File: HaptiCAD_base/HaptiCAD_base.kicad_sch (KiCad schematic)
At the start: 1 part

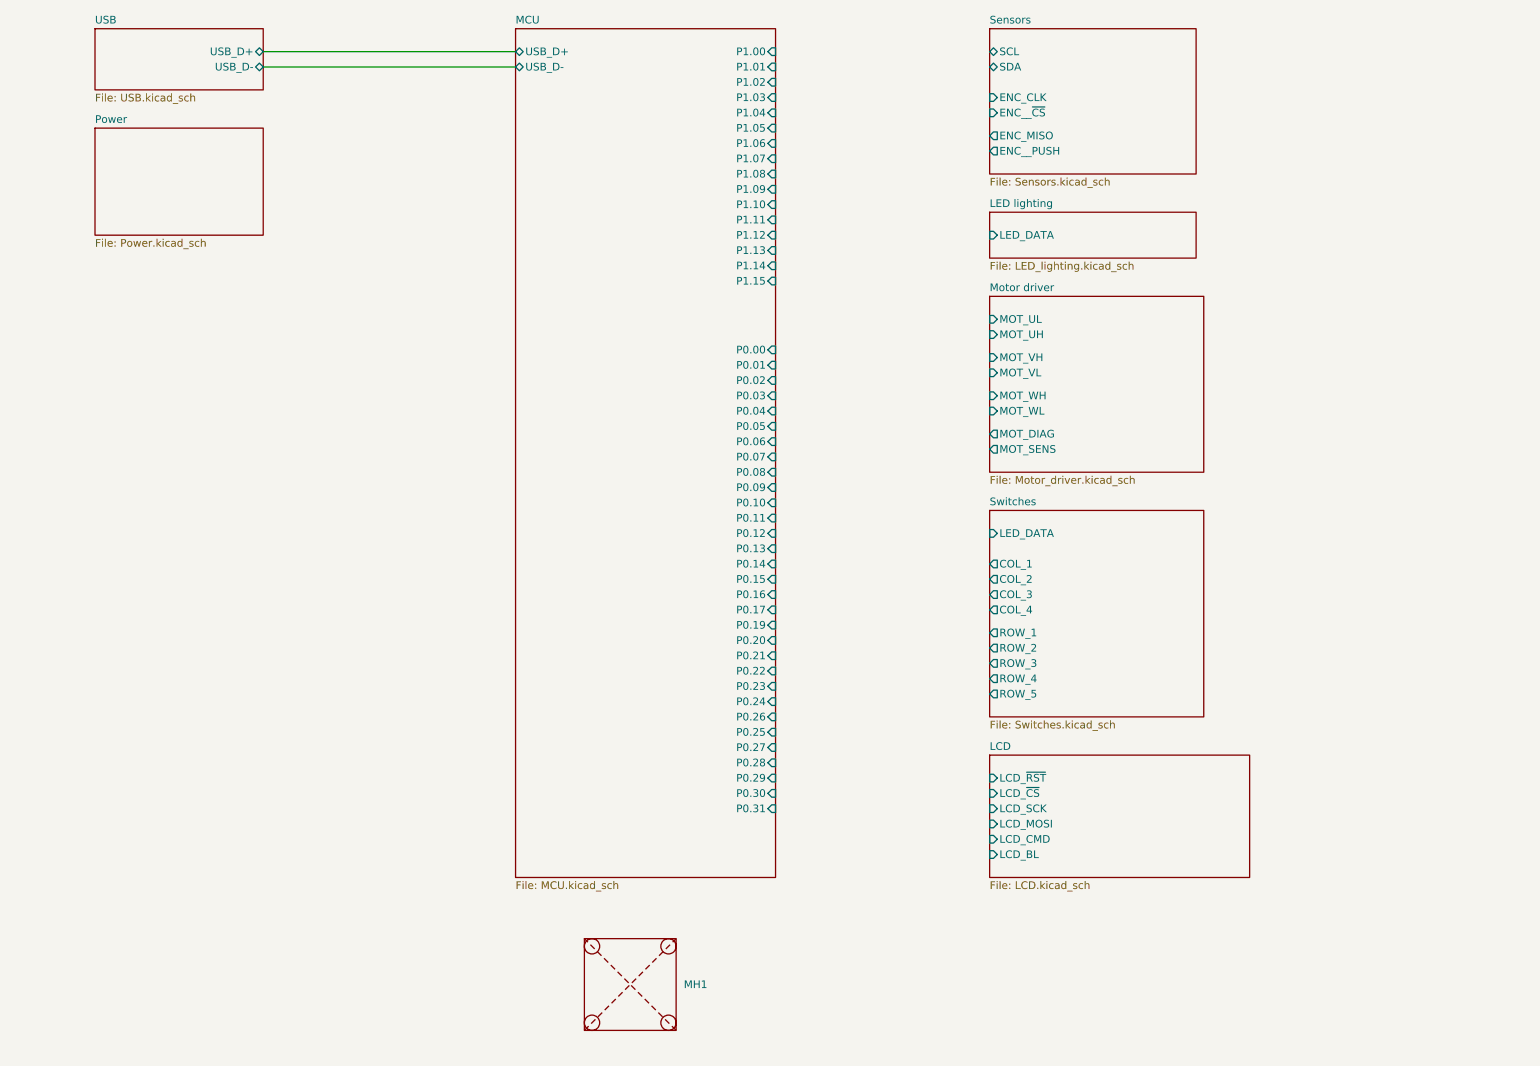
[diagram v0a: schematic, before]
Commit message: Split project into base and motor mount pcb
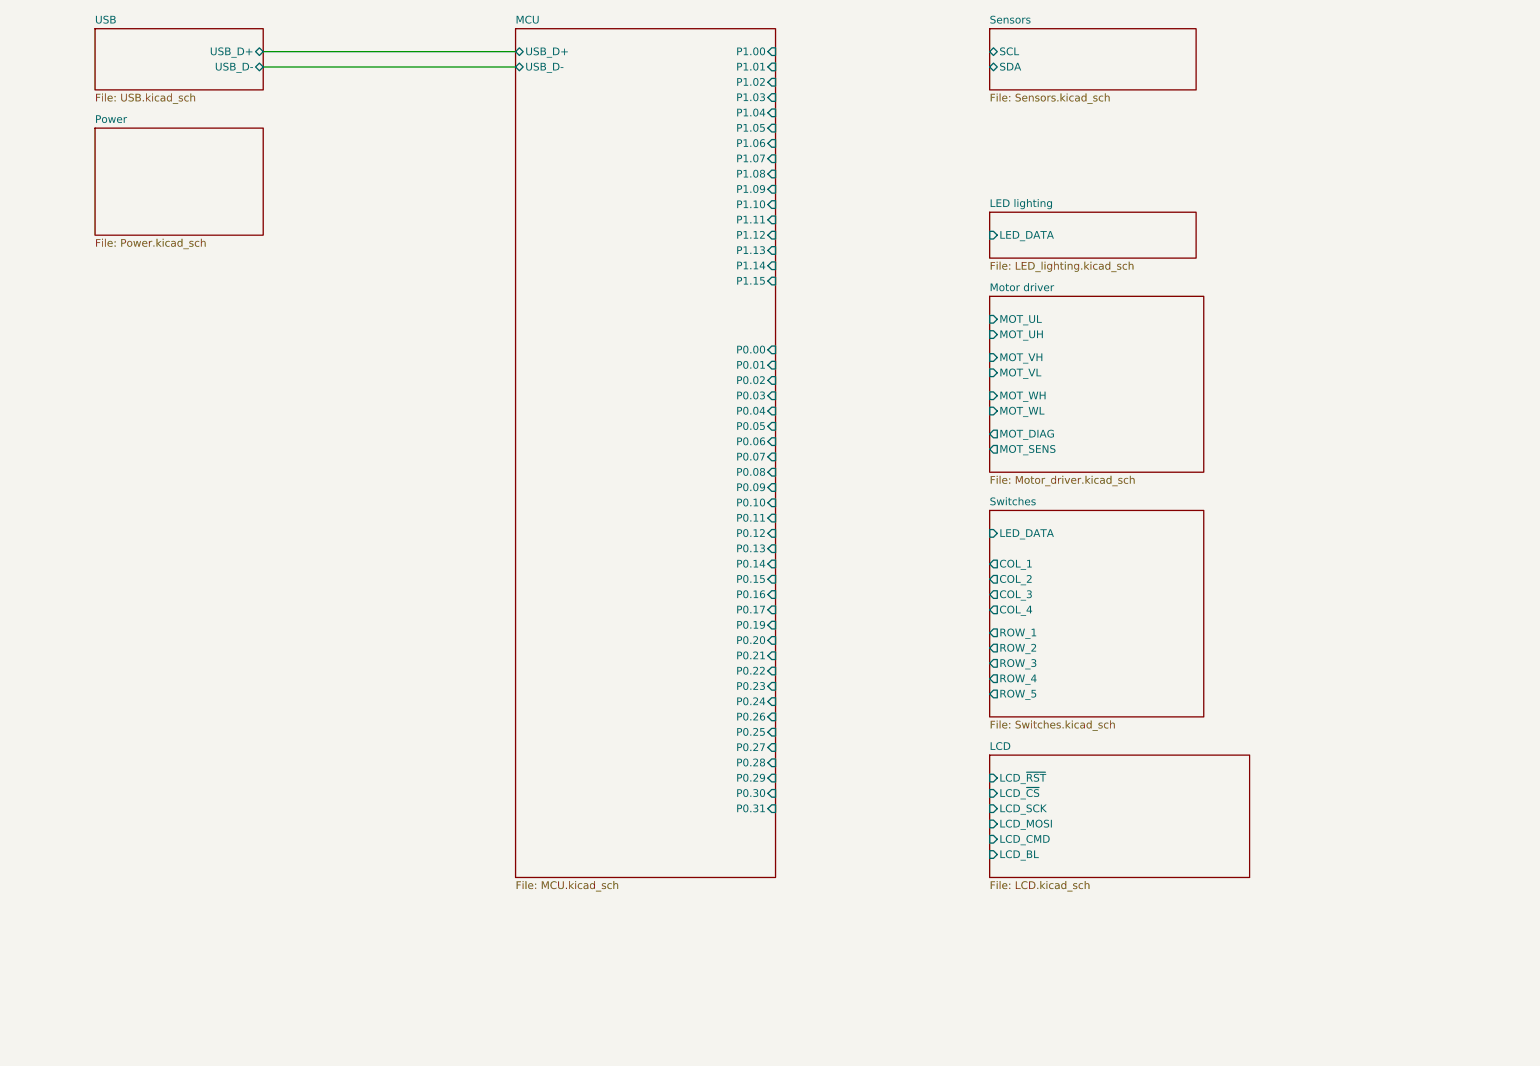
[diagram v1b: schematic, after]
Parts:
- removed MH1: (no value), BLDC_mount:BLDC_mount, symbol BLDC_mount:BLDC_mount
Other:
- sheet Sensors ports: added none; removed ENC_CLK, ENC_MISO, ENC__PUSH, ENC__~{CS}
- title: Knobber -> Base
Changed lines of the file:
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@@
 	(paper "A4")
 	(title_block
-		(title "Knobber")
+		(title "Base")
 		(date "2026-03-16")
 		(rev "V0.1")
@@
 		)
 	)
-	(symbol
-		(lib_id "BLDC_mount:BLDC_mount")
-		(at 135.89 180.34 0)
-		(unit 1)
-		(body_style 1)
-		(exclude_from_sim yes)
+	(sheet
+		(at 195.58 142.24)
+		(size 43.18 20.32)
+		(exclude_from_sim no)
 		(in_bom no)
-		(on_board yes)
-		(in_pos_files yes)
-		(dnp no)
+		(on_board no)
+		(dnp yes)
 		(fields_autoplaced yes)
-		(property "Reference" "MH1"
-			(at 144.78 180.3399 0)
-			(show_name no)
-			(do_not_autoplace no)
-			(effects
-				(font
-					(size 1.27 1.27)
-				)
-				(justify left)
-			)
-		)
-		(property "Value" ""
-			(at 135.89 180.34 0)
-			(show_name no)
-			(do_not_autoplace no)
-			(effects
-				(font
-					(size 1.27 1.27)
-				)
-			)
-		)
-		(property "Footprint" "BLDC_mount:BLDC_mount"
-			(at 135.89 180.34 0)
-			(hide yes)
-			(show_name no)
-			(do_not_autoplace no)
-			(effects
-				(font
-					(size 1.27 1.27)
-				)
-			)
-		)
-		(property "Datasheet" ""
-			(at 135.89 180.34 0)
-			(hide yes)
-			(show_name no)
-			(do_not_autoplace no)
-			(effects
-				(font
-					(size 1.27 1.27)
-				)
-			)
-		)
-		(property "Description" ""
-			(at 135.89 180.34 0)
-			(hide yes)
-			(show_name no)
-			(do_not_autoplace no)
-			(effects
-				(font
-					(size 1.27 1.27)
-				)
+		(stroke
+			(width 0.1524)
+			(type solid)
+		)
+		(fill
+			(color 0 0 0 0)
+		)
+		(property "Sheetname" "LCD"
+			(at 195.58 141.5284 0)
+			(show_name no)
+			(do_not_autoplace no)
+			(effects
+				(font
+					(size 1.27 1.27)
+				)
+				(justify left bottom)
+			)
+		)
+		(property "Sheetfile" "LCD.kicad_sch"
+			(at 195.58 163.1446 0)
+			(show_name no)
+			(do_not_autoplace no)
+			(effects
+				(font
+					(size 1.27 1.27)
+				)
+				(justify left top)
+			)
+		)
+		(pin "LCD_BL" input
+			(at 195.58 158.75 180)
+			(effects
+				(font
+					(size 1.27 1.27)
+				)
+				(justify left)
+			)
+		)
+		(pin "LCD_CMD" input
+			(at 195.58 156.21 180)
+			(effects
+				(font
+					(size 1.27 1.27)
+				)
+				(justify left)
+			)
+		)
+		(pin "LCD_MOSI" input
+			(at 195.58 153.67 180)
+			(effects
+				(font
+					(size 1.27 1.27)
+				)
+				(justify left)
+			)
+		)
+		(pin "LCD_SCK" input
+			(at 195.58 151.13 180)
+			(effects
+				(font
+					(size 1.27 1.27)
+				)
+				(justify left)
+			)
+		)
+		(pin "LCD_~{CS}" input
+			(at 195.58 148.59 180)
+			(effects
+				(font
+					(size 1.27 1.27)
+				)
+				(justify left)
+			)
+		)
+		(pin "LCD_~{RST}" input
+			(at 195.58 146.05 180)
+			(effects
+				(font
+					(size 1.27 1.27)
+				)
+				(justify left)
 			)
 		)
 		(instances
-			(project "knobber"
+			(project "HaptiCAD_base"
 				(path "/09c102b8-dfc1-4666-b1e2-d0c53b401993"
-					(reference "MH1")
-					(unit 1)
+					(page "9")
 				)
 			)
@@
 		)
 		(instances
-			(project "knobber"
+			(project "HaptiCAD_base"
 				(path "/09c102b8-dfc1-4666-b1e2-d0c53b401993"
 					(page "6")
-				)
-			)
-		)
-	)
-	(sheet
-		(at 195.58 142.24)
-		(size 43.18 20.32)
-		(exclude_from_sim no)
-		(in_bom no)
-		(on_board no)
-		(dnp yes)
-		(fields_autoplaced yes)
-		(stroke
-			(width 0.1524)
-			(type solid)
-		)
-		(fill
-			(color 0 0 0 0)
-		)
-		(property "Sheetname" "LCD"
-			(at 195.58 141.5284 0)
-			(show_name no)
-			(do_not_autoplace no)
-			(effects
-				(font
-					(size 1.27 1.27)
-				)
-				(justify left bottom)
-			)
-		)
-		(property "Sheetfile" "LCD.kicad_sch"
-			(at 195.58 163.1446 0)
-			(show_name no)
-			(do_not_autoplace no)
-			(effects
-				(font
-					(size 1.27 1.27)
-				)
-				(justify left top)
-			)
-		)
-		(pin "LCD_BL" input
-			(at 195.58 158.75 180)
-			(effects
-				(font
-					(size 1.27 1.27)
-				)
-				(justify left)
-			)
-		)
-		(pin "LCD_CMD" input
-			(at 195.58 156.21 180)
-			(effects
-				(font
-					(size 1.27 1.27)
-				)
-				(justify left)
-			)
-		)
-		(pin "LCD_MOSI" input
-			(at 195.58 153.67 180)
-			(effects
-				(font
-					(size 1.27 1.27)
-				)
-				(justify left)
-			)
-		)
-		(pin "LCD_SCK" input
-			(at 195.58 151.13 180)
-			(effects
-				(font
-					(size 1.27 1.27)
-				)
-				(justify left)
-			)
-		)
-		(pin "LCD_~{CS}" input
-			(at 195.58 148.59 180)
-			(effects
-				(font
-					(size 1.27 1.27)
-				)
-				(justify left)
-			)
-		)
-		(pin "LCD_~{RST}" input
-			(at 195.58 146.05 180)
-			(effects
-				(font
-					(size 1.27 1.27)
-				)
-				(justify left)
-			)
-		)
-		(instances
-			(project "knobber"
-				(path "/09c102b8-dfc1-4666-b1e2-d0c53b401993"
-					(page "9")
 				)
 			)
@@
 		)
 		(instances
-			(project "knobber"
+			(project "HaptiCAD_base"
 				(path "/09c102b8-dfc1-4666-b1e2-d0c53b401993"
 					(page "2")
@@
 		)
 		(instances
-			(project "knobber"
+			(project "HaptiCAD_base"
 				(path "/09c102b8-dfc1-4666-b1e2-d0c53b401993"
 					(page "7")
@@
 	(sheet
 		(at 195.58 21.59)
-		(size 34.29 24.13)
+		(size 34.29 10.16)
 		(exclude_from_sim no)
 		(in_bom yes)
@@
 		)
 		(property "Sheetfile" "Sensors.kicad_sch"
-			(at 195.58 46.3046 0)
+			(at 195.58 32.3346 0)
 			(show_name no)
 			(do_not_autoplace no)
@@
 			)
 		)
-		(pin "ENC_CLK" input
-			(at 195.58 33.02 180)
-			(effects
-				(font
-					(size 1.27 1.27)
-				)
-				(justify left)
-			)
-		)
-		(pin "ENC_MISO" output
-			(at 195.58 39.37 180)
-			(effects
-				(font
-					(size 1.27 1.27)
-				)
-				(justify left)
-			)
-		)
 		(pin "SDA" bidirectional
 			(at 195.58 27.94 180)
@@
 			)
 		)
-		(pin "ENC__~{CS}" input
-			(at 195.58 35.56 180)
-			(effects
-				(font
-					(size 1.27 1.27)
-				)
-				(justify left)
-			)
-		)
-		(pin "ENC__PUSH" output
-			(at 195.58 41.91 180)
-			(effects
-				(font
-					(size 1.27 1.27)
-				)
-				(justify left)
-			)
-		)
 		(instances
-			(project "knobber"
+			(project "HaptiCAD_base"
 				(path "/09c102b8-dfc1-4666-b1e2-d0c53b401993"
 					(page "4")
@@
 		)
 		(instances
-			(project "knobber"
+			(project "HaptiCAD_base"
 				(path "/09c102b8-dfc1-4666-b1e2-d0c53b401993"
 					(page "5")
@@
 		)
 		(instances
-			(project "knobber"
+			(project "HaptiCAD_base"
 				(path "/09c102b8-dfc1-4666-b1e2-d0c53b401993"
 					(page "3")
@@
 		)
 		(instances
-			(project "knobber"
+			(project "HaptiCAD_base"
 				(path "/09c102b8-dfc1-4666-b1e2-d0c53b401993"
 					(page "8")

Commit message: updated base schematic and PCB
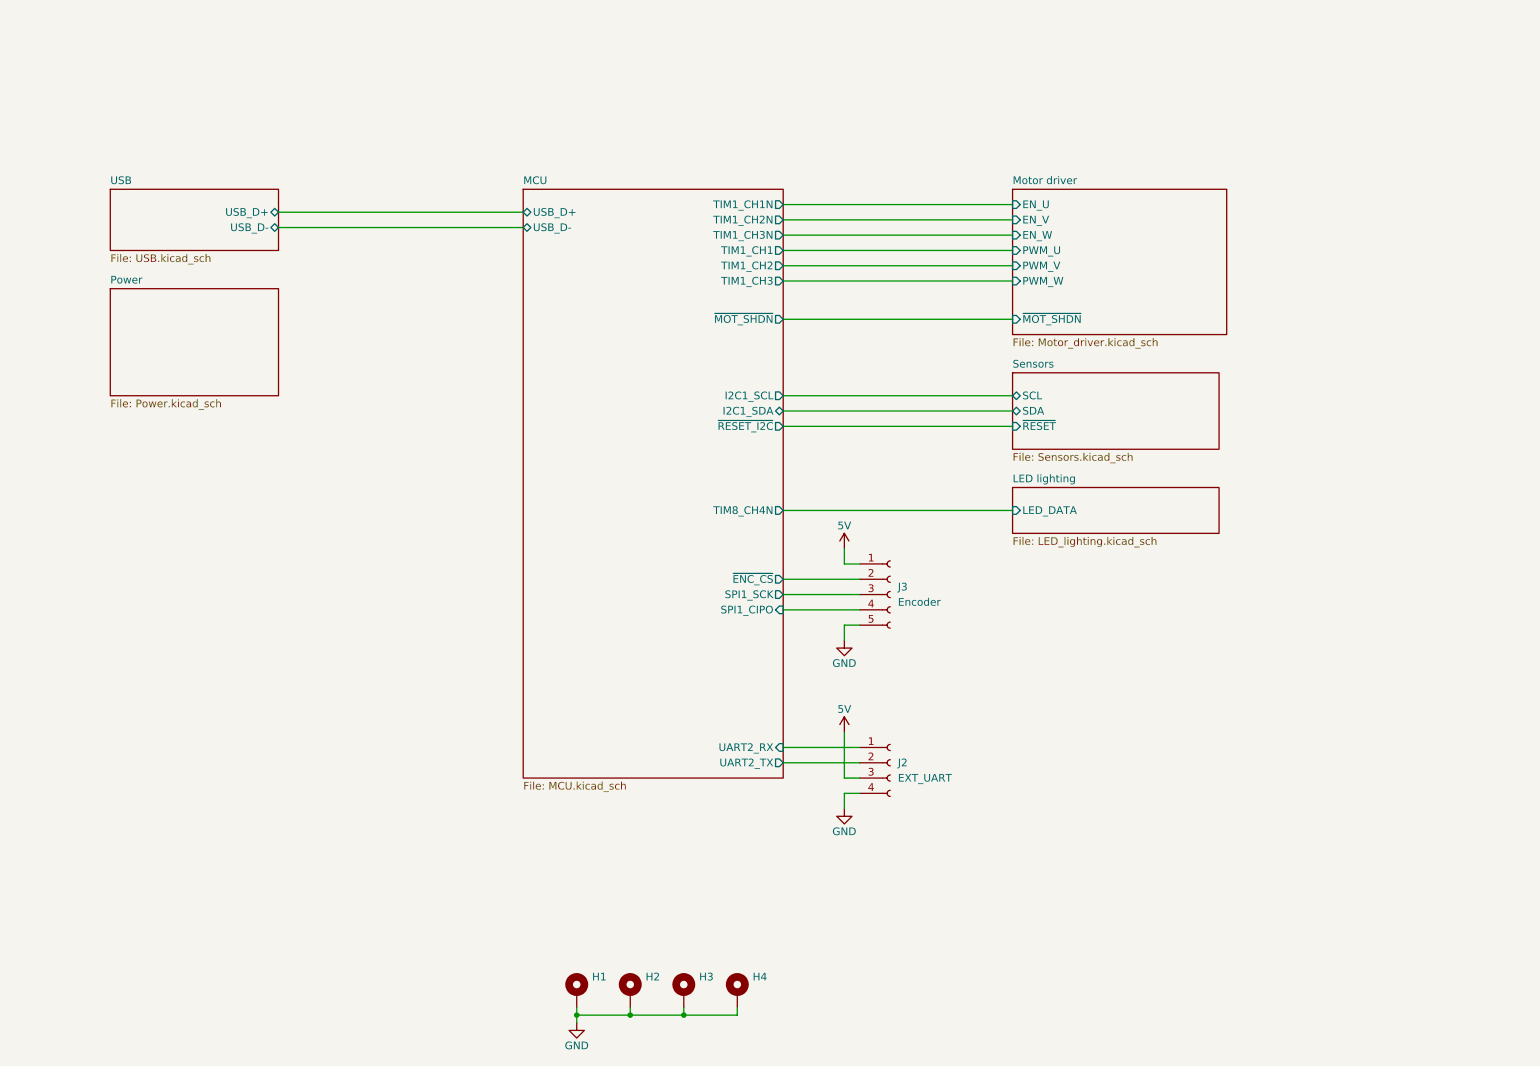
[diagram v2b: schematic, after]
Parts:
- added H1, H2, H3, H4: MountingHole_Pad, MountingHole:MountingHole_3.2mm_M3_DIN965_Pad, symbol Mechanical:MountingHole_Pad
- added J2: EXT_UART, symbol Connector:Conn_01x04_Socket
- added J3: Encoder, symbol Connector:Conn_01x05_Socket
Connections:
- new net 5V: J2.3 (Pin_3), J3.1 (Pin_1)
- new net GND: H1.1, H2.1, H3.1, H4.1, J2.4 (Pin_4), J3.5 (Pin_5)
- new net MCU/SPI1_CIPO: J3.4 (Pin_4)
- new net MCU/SPI1_SCK: J3.3 (Pin_3)
- new net MCU/UART2_RX: J2.1 (Pin_1)
- new net MCU/UART2_TX: J2.2 (Pin_2)
- new net MCU/~{ENC_CS}: J3.2 (Pin_2)
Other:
- removed sheet LCD
- removed sheet Switches
- sheet MCU ports: added I2C1_SCL, I2C1_SDA, SPI1_CIPO, SPI1_SCK, TIM1_CH1, TIM1_CH1N, TIM1_CH2, TIM1_CH2N, TIM1_CH3, TIM1_CH3N, TIM8_CH4N, UART2_RX, UART2_TX, ~{ENC_CS}, ~{MOT_SHDN}, ~{RESET_I2C}; removed P0.00, P0.01, P0.02, P0.03, P0.04, P0.05, P0.06, P0.07, P0.08, P0.09, P0.10, P0.11, P0.12, P0.13, P0.14, P0.15, P0.16, P0.17, P0.19, P0.20, P0.21, P0.22, P0.23, P0.24, P0.25, P0.26, P0.27, P0.28, P0.29, P0.30, P0.31, P1.00, P1.01, P1.02, P1.03, P1.04, P1.05, P1.06, P1.07, P1.08, P1.09, P1.10, P1.11, P1.12, P1.13, P1.14, P1.15
- sheet Motor driver ports: added EN_U, EN_V, EN_W, PWM_U, PWM_V, PWM_W, ~{MOT_SHDN}; removed MOT_DIAG, MOT_SENS, MOT_UH, MOT_UL, MOT_VH, MOT_VL, MOT_WH, MOT_WL
- sheet Sensors ports: added ~{RESET}; removed none

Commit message: Finished schematic of the base board
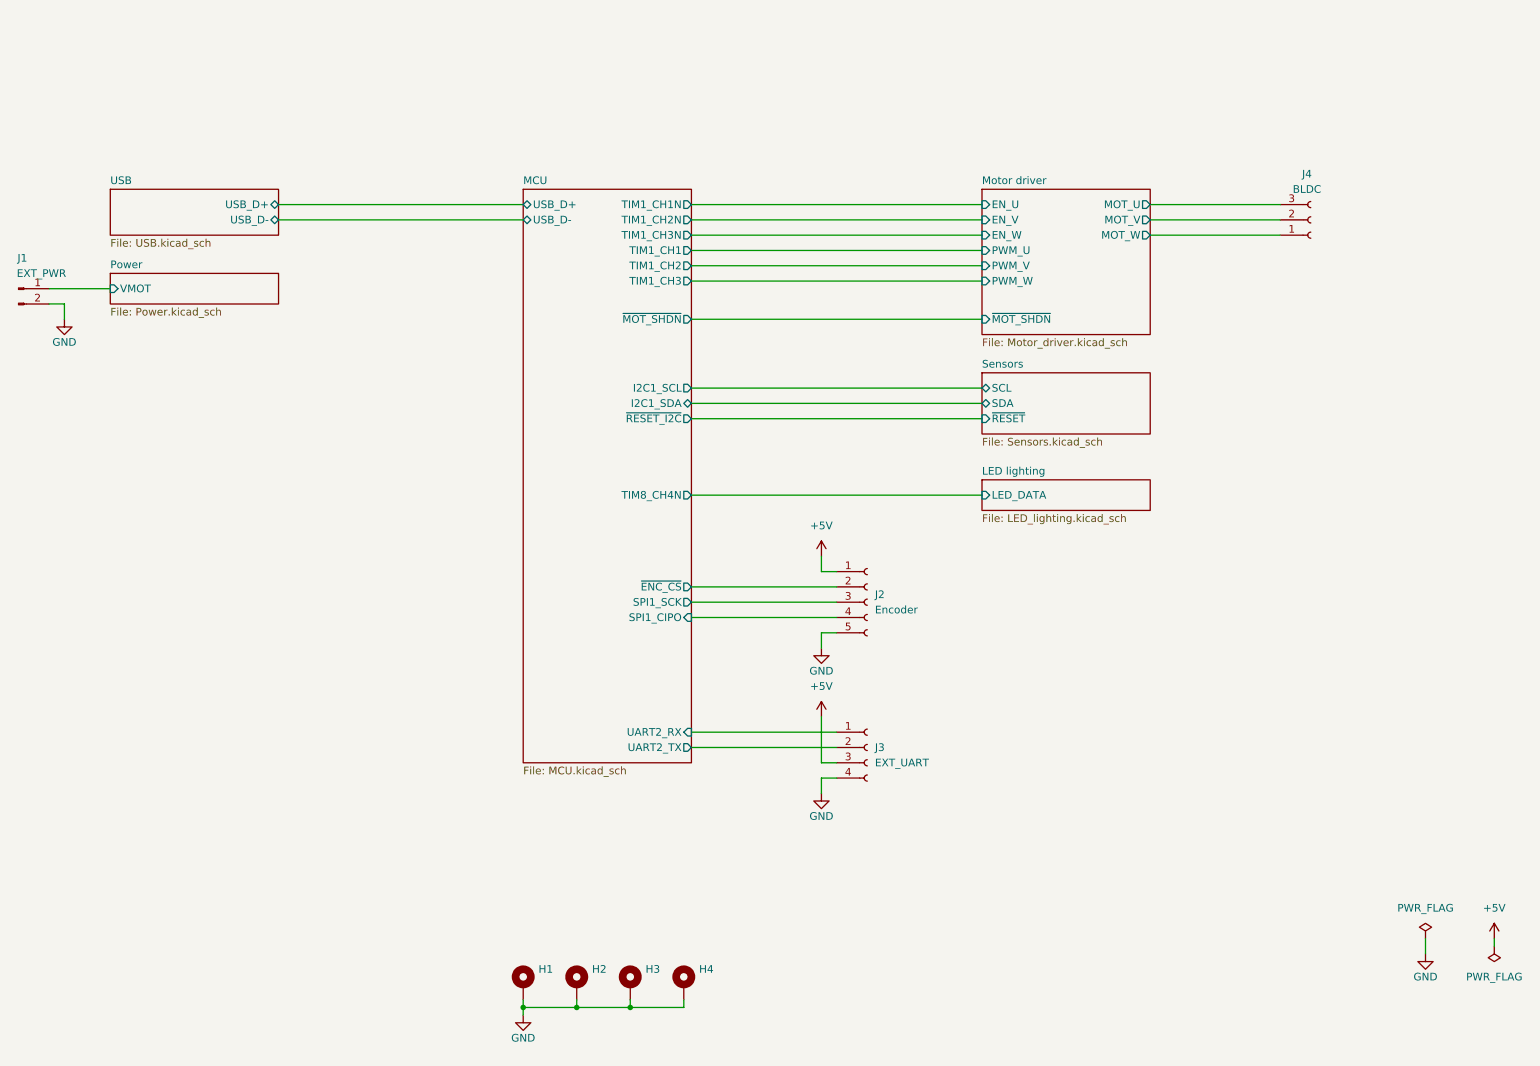
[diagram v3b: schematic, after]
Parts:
- added J1: EXT_PWR, symbol Connector:Conn_01x02_Pin
- added J4: BLDC, Connector_Molex:Molex_SPOX_5267-03A_1x03_P2.50mm_Vertical, symbol Connector:Conn_01x03_Socket
- renumbered J3 to J2, J2 to J3
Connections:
- net GND: now also J1.2 (Pin_2)
- net 5V renamed +5V
- new net Motor driver/MOT_U: J4.3 (Pin_3)
- new net Motor driver/MOT_V: J4.2 (Pin_2)
- new net Motor driver/MOT_W: J4.1 (Pin_1)
- new net Power/VMOT: J1.1 (Pin_1)
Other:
- sheet Motor driver ports: added MOT_U, MOT_V, MOT_W; removed none
- sheet Power ports: added VMOT; removed none
- moved on the sheet: H1, H2, H3, H4, J2, J3
